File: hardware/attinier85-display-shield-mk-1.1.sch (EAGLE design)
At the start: 5 parts, among them U1 ATTINIEST85_SHIELDV2

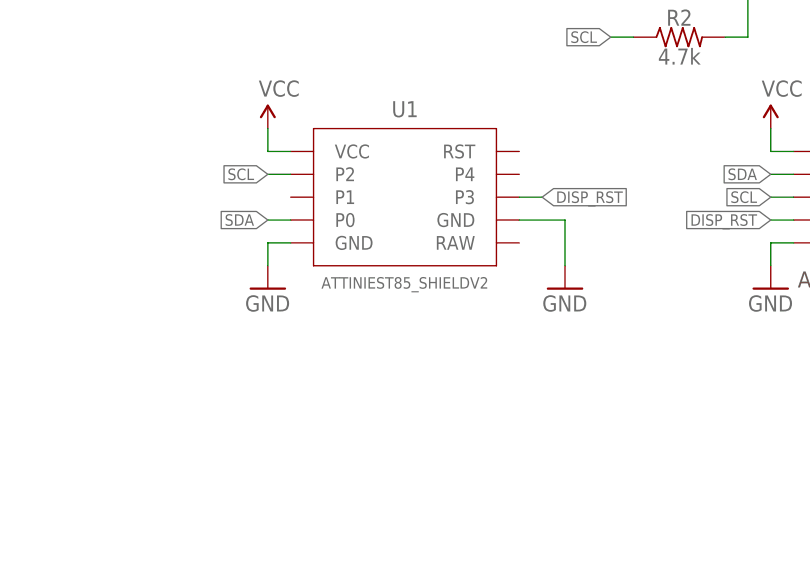
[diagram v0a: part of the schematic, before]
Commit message: renaming parts
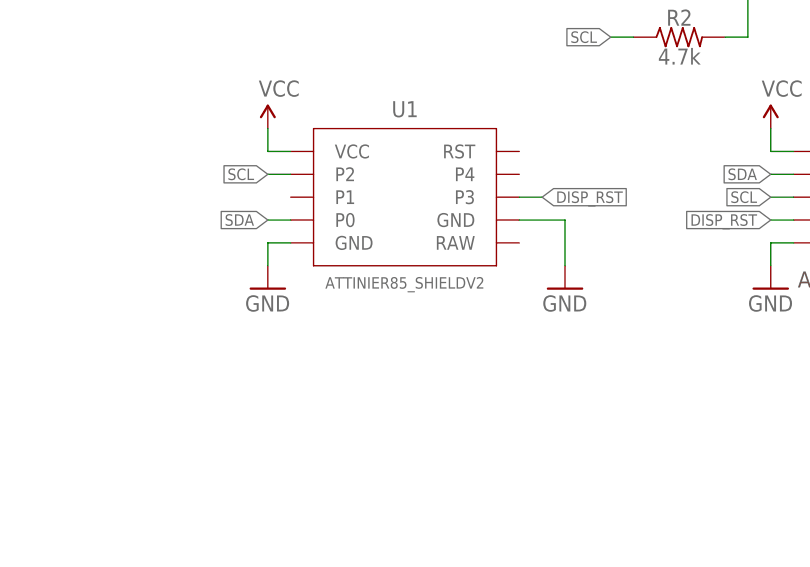
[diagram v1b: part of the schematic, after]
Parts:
- U1: value ATTINIEST85_SHIELDV2 -> ATTINIER85_SHIELDV2; device A_butts:ATTINIEST85_SHIELDV2 -> A_butts:ATTINIER85_SHIELDV2
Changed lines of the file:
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@@
 <parts>
 <part name="FRAME1" library="A_butts" deviceset="FRAME-LETTER" device="NO_PACKAGE"/>
-<part name="U1" library="A_butts" deviceset="ATTINIEST85_SHIELD" device="V2"/>
+<part name="U1" library="A_butts" deviceset="ATTINIER85_SHIELD" device="V2"/>
 <part name="SUPPLY1" library="A_butts" deviceset="VCC" device=""/>
 <part name="GND1" library="A_butts" deviceset="GND" device=""/>
